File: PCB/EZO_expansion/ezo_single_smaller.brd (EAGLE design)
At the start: 66 x 30.5 mm, 7 parts

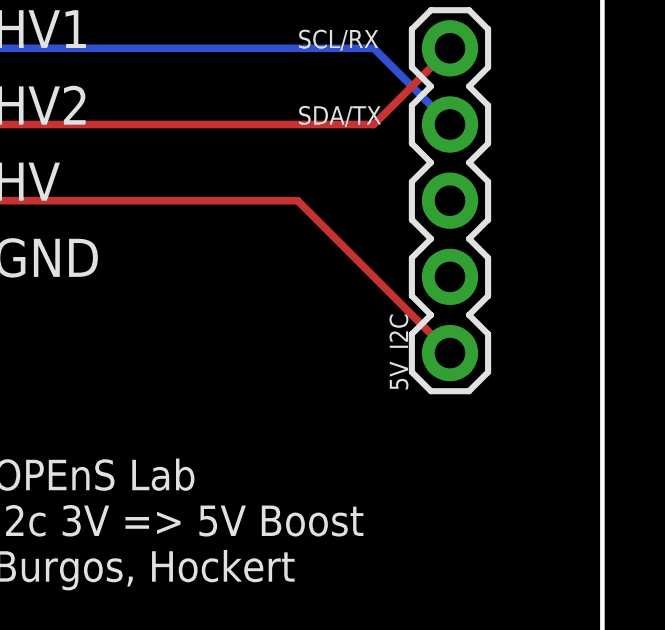
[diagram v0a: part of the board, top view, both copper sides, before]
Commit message: Tied the OFF Pin on the EZO Isolated Carrier board to high, hopefully fixing our issues of fried DO circuits
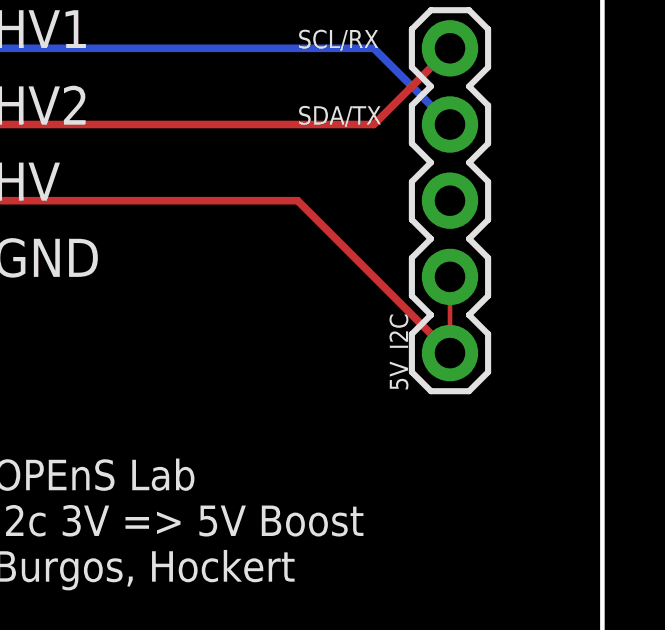
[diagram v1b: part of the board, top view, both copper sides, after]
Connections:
- net 5V: now also 5V_I2C.2
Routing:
- net 5V: track 61.1 -> 63.7 mm
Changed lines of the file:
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@@
 <wire x1="40.64" y1="15.24" x2="55.88" y2="15.24" width="0.254" layer="1"/>
 <wire x1="55.88" y1="15.24" x2="60.96" y2="10.16" width="0.254" layer="1"/>
+<contactref element="5V_I2C" pad="2"/>
+<wire x1="60.96" y1="10.16" x2="60.96" y2="12.7" width="0.1524" layer="1"/>
 </signal>
 <signal name="3.3V">
